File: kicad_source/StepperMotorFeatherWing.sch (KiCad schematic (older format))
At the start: 10 parts, among them CN1 ADAFRUIT_FEATHER, P10 CONN_01X04, P7 CONN_01X04, P8 CONN_01X04, P9 CONN_01X04

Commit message: generated pdf files
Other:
- note added: "Copyright generationmake 2019\nsee full project documentation at https://github.com/generationmake/StepperMotorFeatherWing"
- note removed: "Copyright generationmake 2019\nsee full project documentation at http://arduhmi.generationmake.de"
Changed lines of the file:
@@
 Sheet 1 6
 Title "HighPowerMotorFeatherWing"
-Date "2019-12-01"
+Date "2019-12-31"
 Rev "1.0"
 Comp "generationmake"
@@
 $EndDescr
 Text Notes 500  650  0    47   ~ 0
-Copyright generationmake 2019\nsee full project documentation at http://arduhmi.generationmake.de
+Copyright generationmake 2019\nsee full project documentation at https://github.com/generationmake/StepperMotorFeatherWing
 Text Notes 7000 6900 0    43   ~ 0
 You may redistribute and modify this documentation under the terms of the CERN OHL v.1.2. (http://ohwr.org/cernohl). \nThis documentation is distributed WITHOUT ANY EXPRESS OR IMPLIED WARRANTY, INCLUDING OF MERCHANTABILITY, SATISFACTORY \nQUALITY AND FITNESS FOR A PARTICULAR PURPOSE. Please see the CERN OHL v.1.2  for applicable conditions

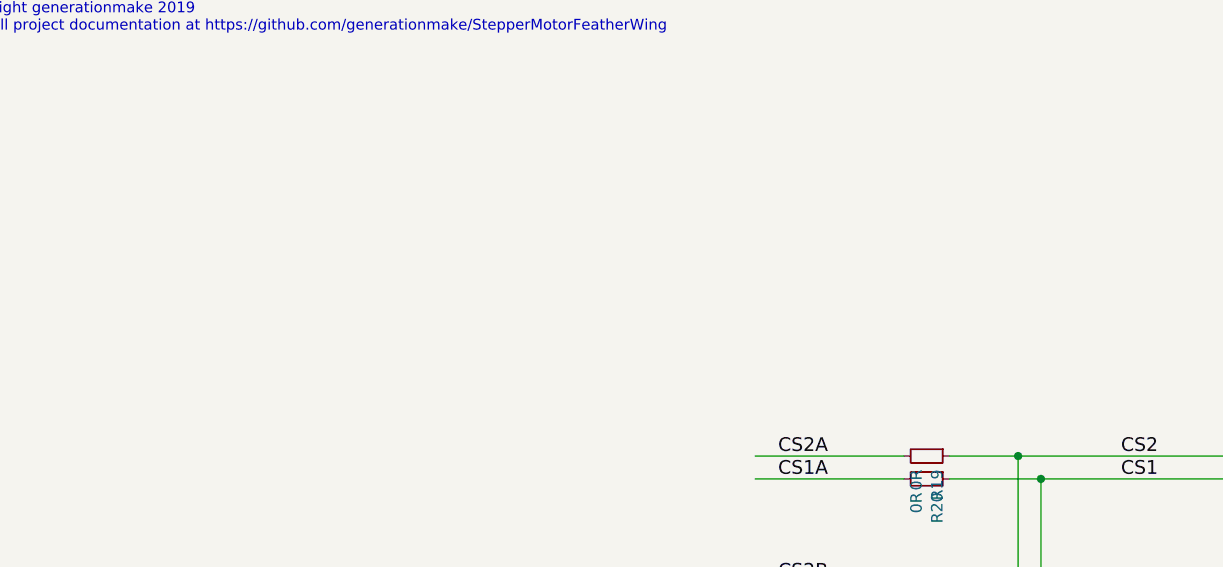
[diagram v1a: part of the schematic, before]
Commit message: added clock generator as common clock for both stepper drivers
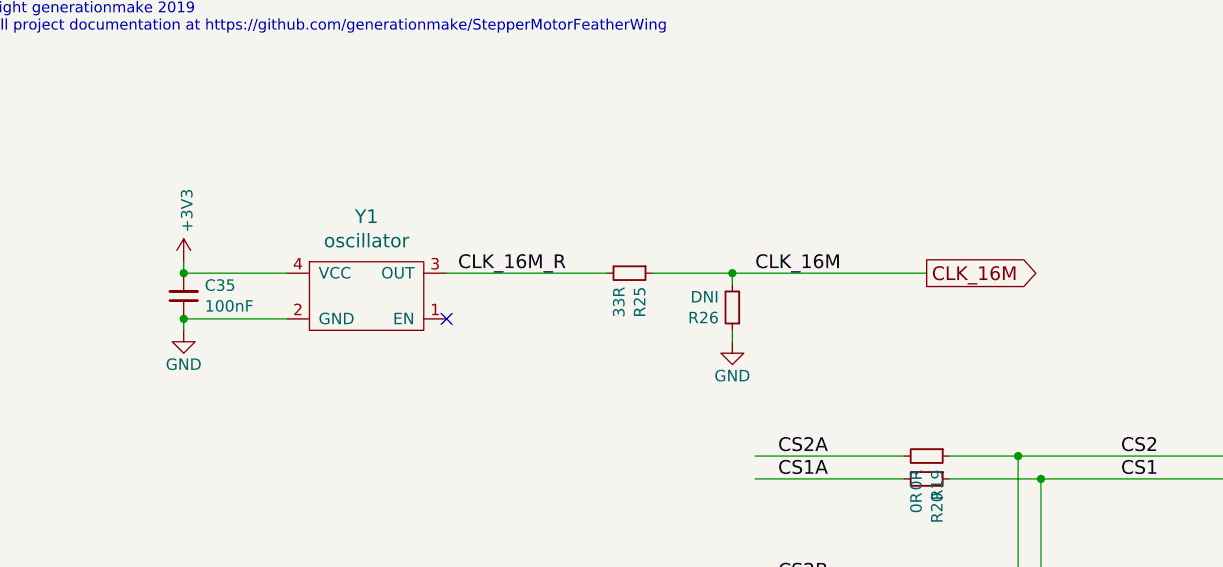
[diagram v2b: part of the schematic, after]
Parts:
- added C35: 100nF, capacitors:C_0603, symbol devices:C_0603
- added R25: 33R, resistors:R_0603, symbol devices:R_0603
- added R26: DNI, resistors:R_0603, symbol devices:R_0603
- added Y1: oscillator, crystals:Crystal_SMD_3.2x2.5mm_4Pad, symbol devices:oscillator
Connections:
- net labels added: CLK_16M, CLK_16M_R
- wire segments 57 -> 66
- no-connect marks 11 -> 12
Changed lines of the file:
@@
+$EndSheet
+$Sheet
+S 7000 1000 1000 500
+U 5DEC41AF
+F0 "MotorDriver1" 60
+F1 "MotorDriver1.sch" 60
+$EndSheet
+$Sheet
+S 7000 2000 1000 500
+U 5DE3616E
+F0 "MotorDriver2" 60
+F1 "MotorDriver2.sch" 60
 $EndSheet
 $Sheet
@@
 NoConn ~ 4000 4650
 NoConn ~ 4000 4550
-$Sheet
-S 7000 2000 1000 500
-U 5DE3616E
-F0 "MotorDriver2" 60
-F1 "MotorDriver2.sch" 60
-$EndSheet
-$Sheet
-S 7000 1000 1000 500
-U 5DEC41AF
-F0 "MotorDriver1" 60
-F1 "MotorDriver1.sch" 60
-$EndSheet
 Text GLabel 6150 2500 2    60   Output ~ 0
 CS2
@@
 Text Label 4100 5050 0    60   ~ 0
 CS1A
+$Comp
+L devices:oscillator Y1
+U 1 1 5F0010B3
+P 2300 1800
+F 0 "Y1" H 2300 2147 60  0000 C CNN
+F 1 "oscillator" H 2300 2041 60  0000 C CNN
+F 2 "crystals:Crystal_SMD_3.2x2.5mm_4Pad" H 2300 1800 60  0001 C CNN
+F 3 "" H 2300 1800 60  0001 C CNN
+	1    2300 1800
+	1    0    0    -1
+$EndComp
+$Comp
+L devices:R_0603 R25
+U 1 1 5F001947
+P 3450 1700
+F 0 "R25" H 3509 1746 50  0000 L CNN
+F 1 "33R" H 3509 1655 50  0000 L CNN
+F 2 "resistors:R_0603" H 3450 1550 50  0001 C CNN
+F 3 "" H 3450 1700 50  0000 C CNN
+	1    3450 1700
+	0    1    1    0
+$EndComp
+$Comp
+L devices:R_0603 R26
+U 1 1 5F001C97
+P 3900 1850
+F 0 "R26" H 3959 1896 50  0000 L CNN
+F 1 "DNI" H 3959 1805 50  0000 L CNN
+F 2 "resistors:R_0603" H 3900 1700 50  0001 C CNN
+F 3 "" H 3900 1850 50  0000 C CNN
+	1    3900 1850
+	-1   0    0    1
+$EndComp
+$Comp
+L devices:C_0603 C35
+U 1 1 5F0028F4
+P 1500 1800
+F 0 "C35" H 1408 1754 50  0000 R CNN
+F 1 "100nF" H 1408 1845 50  0000 R CNN
+F 2 "capacitors:C_0603" H 1500 1650 50  0001 C CNN
+F 3 "" H 1500 1800 50  0000 C CNN
+	1    1500 1800
+	-1   0    0    1
+$EndComp
+$Comp
+L StepperMotorFeatherWing-rescue:+3V3-power-supply-MKRHMIShield-rescue-MKRHMIShield-rescue-HMIFeatherWing-rescue-HighPowerMotorFeatherWing-rescue #PWR095
+U 1 1 5F0037BE
+P 1500 1650
+F 0 "#PWR095" H 1500 1500 50  0001 C CNN
+F 1 "+3V3" V 1515 1778 50  0000 L CNN
+F 2 "" H 1500 1650 50  0000 C CNN
+F 3 "" H 1500 1650 50  0000 C CNN
+	1    1500 1650
+	1    0    0    -1
+$EndComp
+$Comp
+L StepperMotorFeatherWing-rescue:GND-ArduHMIShield-rescue-ArduHMIShield-rescue-MKRHMIShield-rescue-MKRHMIShield-rescue-HMIFeatherWing-rescue-HighPowerMotorFeatherWing-rescue #PWR096
+U 1 1 5F00433B
+P 1500 1950
+F 0 "#PWR096" H 1500 1700 50  0001 C CNN
+F 1 "GND" H 1500 1800 50  0000 C CNN
+F 2 "" H 1500 1950 50  0000 C CNN
+F 3 "" H 1500 1950 50  0000 C CNN
+	1    1500 1950
+	1    0    0    -1
+$EndComp
+$Comp
+L StepperMotorFeatherWing-rescue:GND-ArduHMIShield-rescue-ArduHMIShield-rescue-MKRHMIShield-rescue-MKRHMIShield-rescue-HMIFeatherWing-rescue-HighPowerMotorFeatherWing-rescue #PWR097
+U 1 1 5F00490C
+P 3900 2000
+F 0 "#PWR097" H 3900 1750 50  0001 C CNN
+F 1 "GND" H 3900 1850 50  0000 C CNN
+F 2 "" H 3900 2000 50  0000 C CNN
+F 3 "" H 3900 2000 50  0000 C CNN
+	1    3900 2000
+	1    0    0    -1
+$EndComp
+Wire Wire Line
+	3900 1750 3900 1700
+Connection ~ 3900 1700
+Wire Wire Line
+	3900 1700 3550 1700
+Wire Wire Line
+	3900 1950 3900 2000
+Wire Wire Line
+	1500 1650 1500 1700
+Wire Wire Line
+	1500 1900 1500 1950
+Wire Wire Line
+	1950 1900 1500 1900
+Connection ~ 1500 1900
+Wire Wire Line
+	1950 1700 1500 1700
+Connection ~ 1500 1700
+NoConn ~ 2650 1900
+Wire Wire Line
+	3900 1700 4750 1700
+Wire Wire Line
+	2650 1700 3350 1700
+Text Label 4000 1700 0    60   ~ 0
+CLK_16M
+Text Label 2700 1700 0    60   ~ 0
+CLK_16M_R
+Text GLabel 4750 1700 2    60   Output ~ 0
+CLK_16M
 $EndSCHEMATC

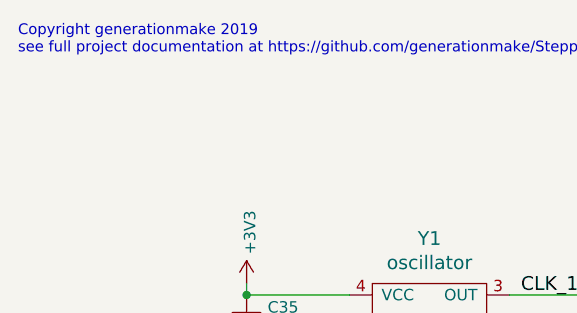
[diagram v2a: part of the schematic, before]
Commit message: added leds and decoupling capacitors
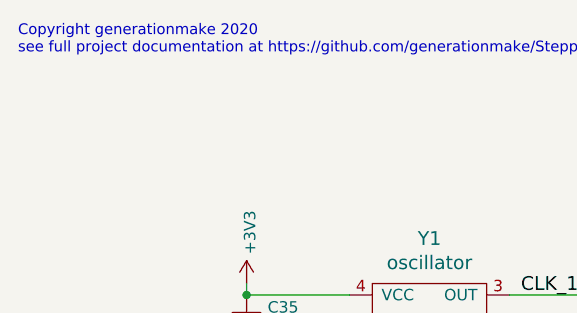
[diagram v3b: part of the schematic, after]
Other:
- note added: "Copyright generationmake 2020\nsee full project documentation at https://github.com/generationmake/StepperMotorFeatherWing"
- note removed: "Copyright generationmake 2019\nsee full project documentation at https://github.com/generationmake/StepperMotorFeatherWing"
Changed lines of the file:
@@
 Sheet 1 6
 Title "HighPowerMotorFeatherWing"
-Date "2019-12-31"
-Rev "1.0"
+Date "2020-07-04"
+Rev "1.1"
 Comp "generationmake"
 Comment1 ""
@@
 $EndDescr
 Text Notes 500  650  0    47   ~ 0
-Copyright generationmake 2019\nsee full project documentation at https://github.com/generationmake/StepperMotorFeatherWing
+Copyright generationmake 2020\nsee full project documentation at https://github.com/generationmake/StepperMotorFeatherWing
 Text Notes 7000 6900 0    43   ~ 0
 You may redistribute and modify this documentation under the terms of the CERN OHL v.1.2. (http://ohwr.org/cernohl). \nThis documentation is distributed WITHOUT ANY EXPRESS OR IMPLIED WARRANTY, INCLUDING OF MERCHANTABILITY, SATISFACTORY \nQUALITY AND FITNESS FOR A PARTICULAR PURPOSE. Please see the CERN OHL v.1.2  for applicable conditions

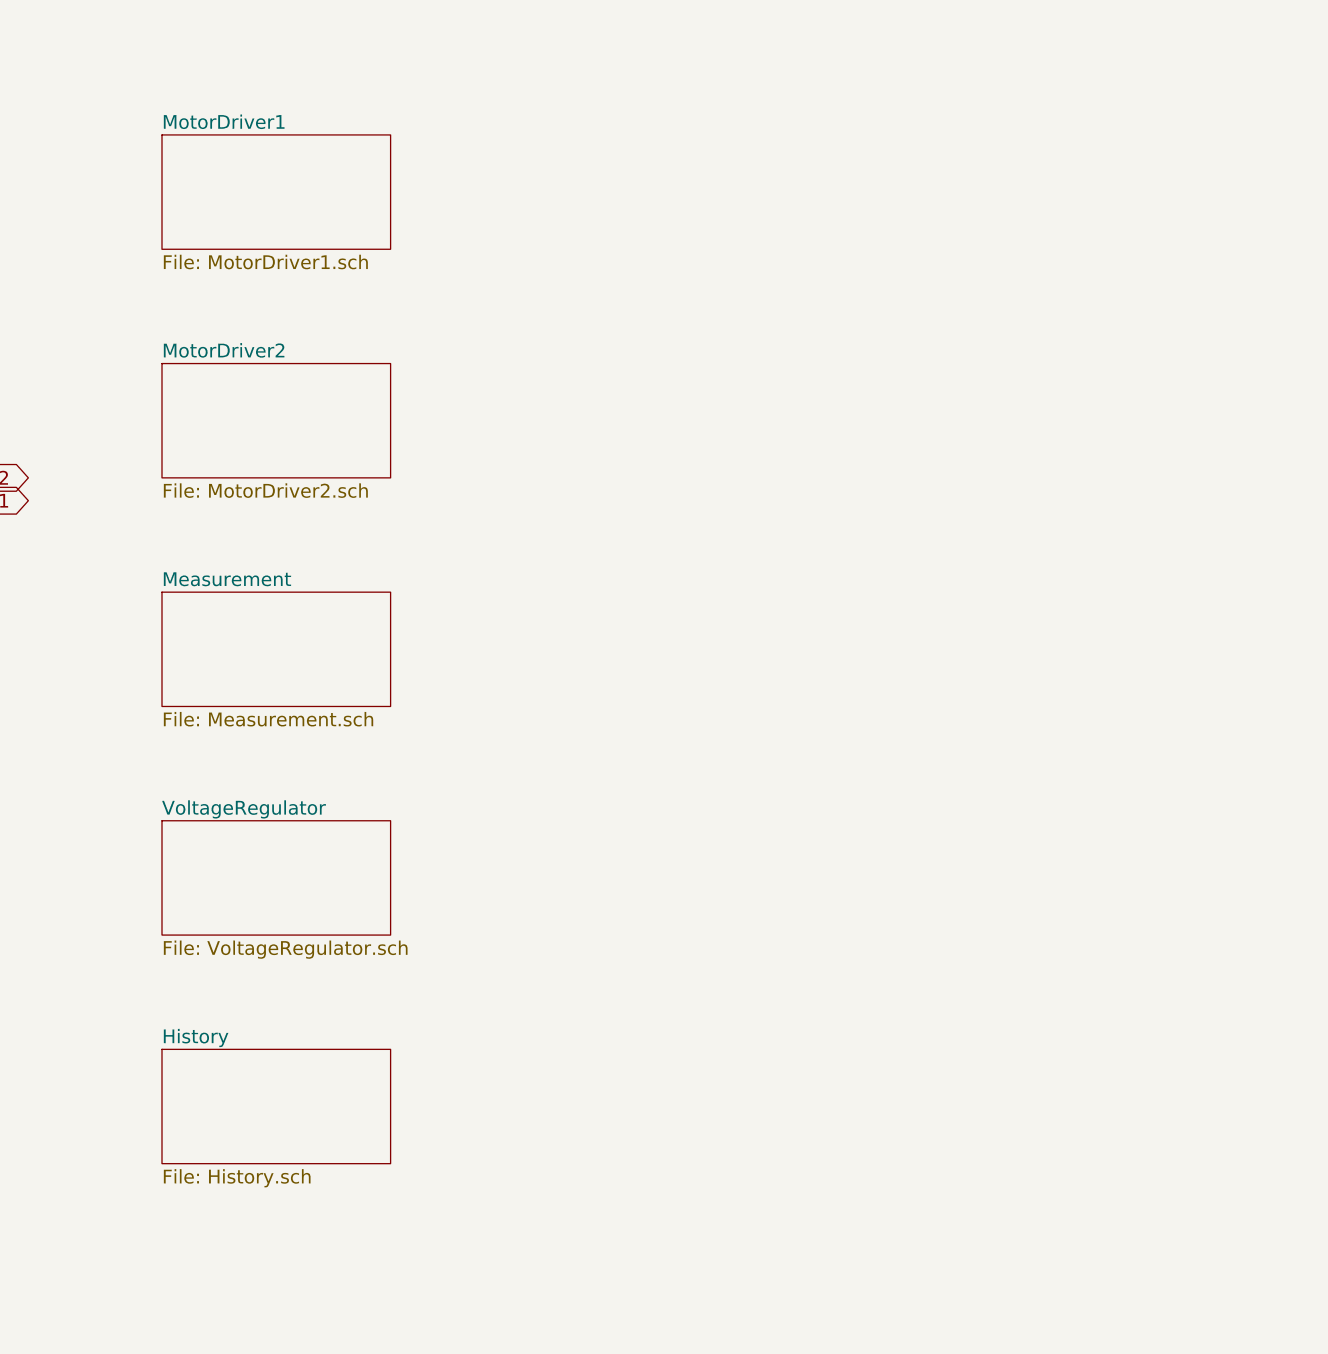
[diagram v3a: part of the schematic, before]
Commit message: added temperature sensor LM75
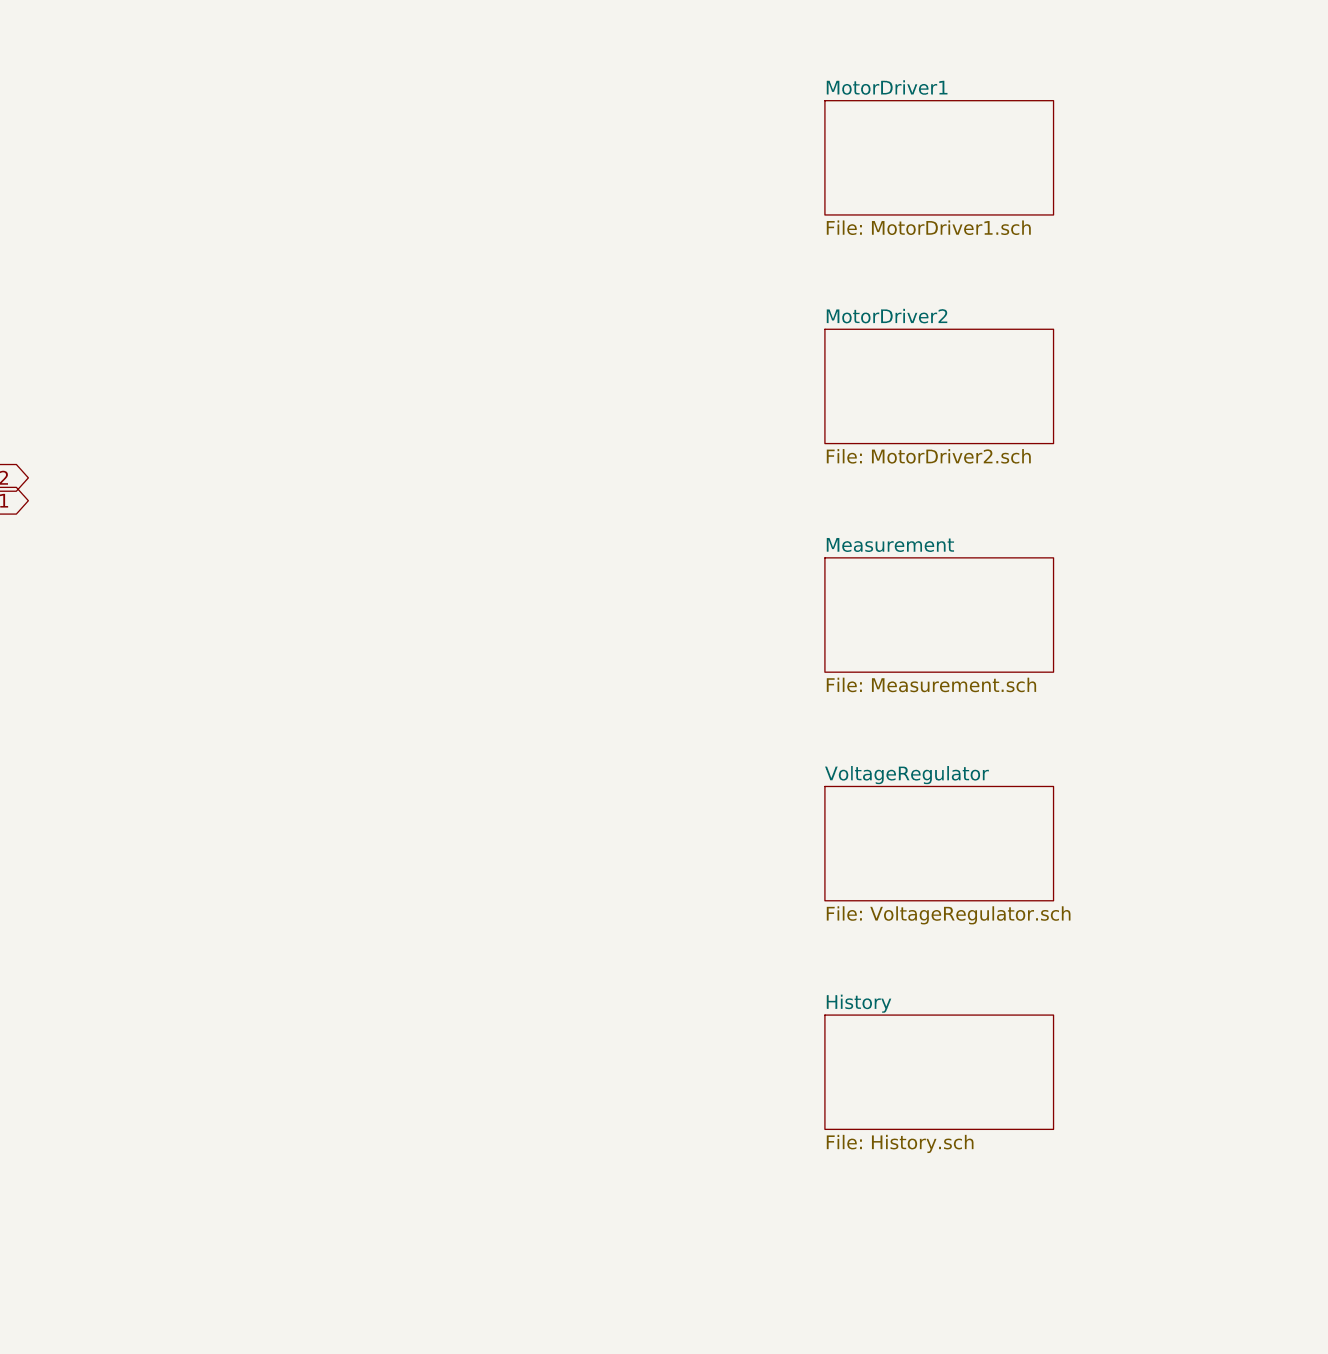
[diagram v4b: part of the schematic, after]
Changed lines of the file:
@@
 I2C_SDA
 $Sheet
-S 7000 3000 1000 500
+S 9900 2850 1000 500
 U 5DE3661B
 F0 "Measurement" 60
@@
 NoConn ~ 2800 5250
 $Sheet
-S 7000 4000 1000 500
+S 9900 3850 1000 500
 U 5DE38154
 F0 "VoltageRegulator" 60
@@
 $EndSheet
 $Sheet
-S 7000 1000 1000 500
+S 9900 850  1000 500
 U 5DEC41AF
 F0 "MotorDriver1" 60
@@
 $EndSheet
 $Sheet
-S 7000 2000 1000 500
+S 9900 1850 1000 500
 U 5DE3616E
 F0 "MotorDriver2" 60
@@
 $EndSheet
 $Sheet
-S 7000 5000 1000 500
+S 9900 4850 1000 500
 U 5DE38FE7
 F0 "History" 60
